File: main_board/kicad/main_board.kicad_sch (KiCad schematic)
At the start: 6 parts, among them J1 Conn_01x02_Pin, J2 Conn_02x30_Odd_Even, U1 Teensy4.1, U2 5V

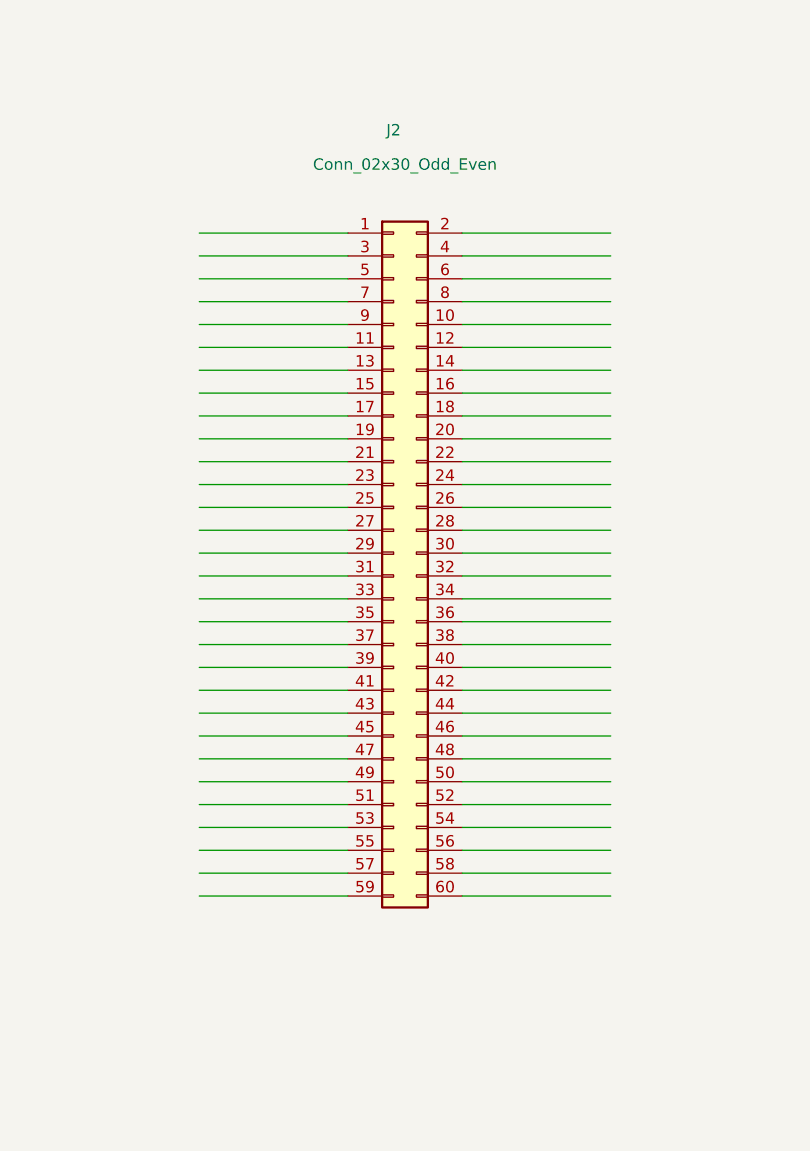
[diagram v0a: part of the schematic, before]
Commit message: Added pcie edge footprint.
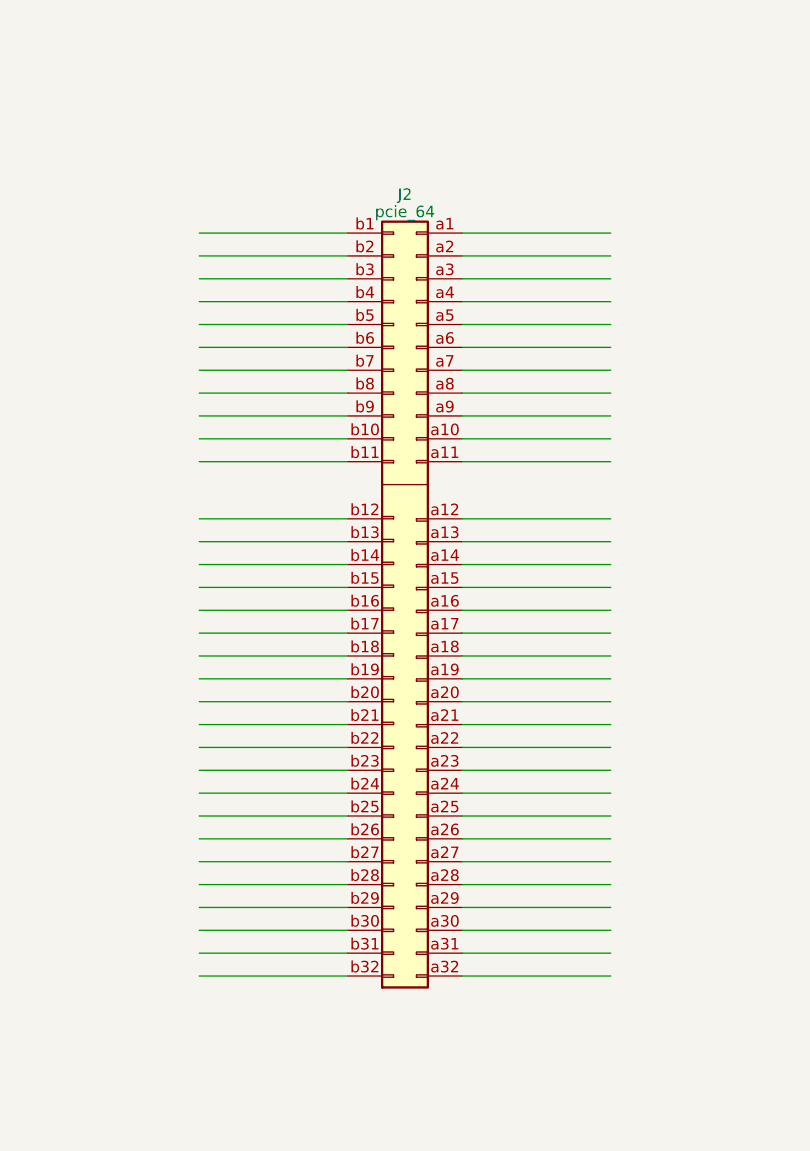
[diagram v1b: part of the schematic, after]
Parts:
- removed J2: Conn_02x30_Odd_Even, symbol Connector_Generic:Conn_02x30_Odd_Even
- added J2: pcie_64, main_board:pcie_64, symbol main_board:pcie_64

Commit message: Progress with main board footprints.
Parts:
- removed D1, D2: D_Schottky, symbol Device:D_Schottky
- removed J1: Conn_01x02_Pin, symbol Connector:Conn_01x02_Pin
- removed J2: pcie_64, main_board:pcie_64, symbol main_board:pcie_64
- removed U1: Teensy4.1, main_board:Teensy41, symbol main_board:Teensy4.1
- removed U2: 5V, Package_TO_SOT_SMD:TO-252-3_TabPin2, symbol Regulator_Linear:IFX27001TFV
- added J1, J2, J3, J4, J5: pcie_98, main_board:pcie_98_socket, symbol main_board:pcie_98
- added RN1: R_Pack06, main_board:weact_stm32fh750, symbol Device:R_Pack06
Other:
- note removed: "EXTERNAL 24V"
- note removed: "MUST CUT TEENSY'S VIN TRACE"
